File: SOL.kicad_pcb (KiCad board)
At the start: 2 copper layers, 50.8 x 31.8 mm, 4 parts, among them J2 Conn_Coaxial, J3 Conn_Coaxial, J4 Conn_Coaxial

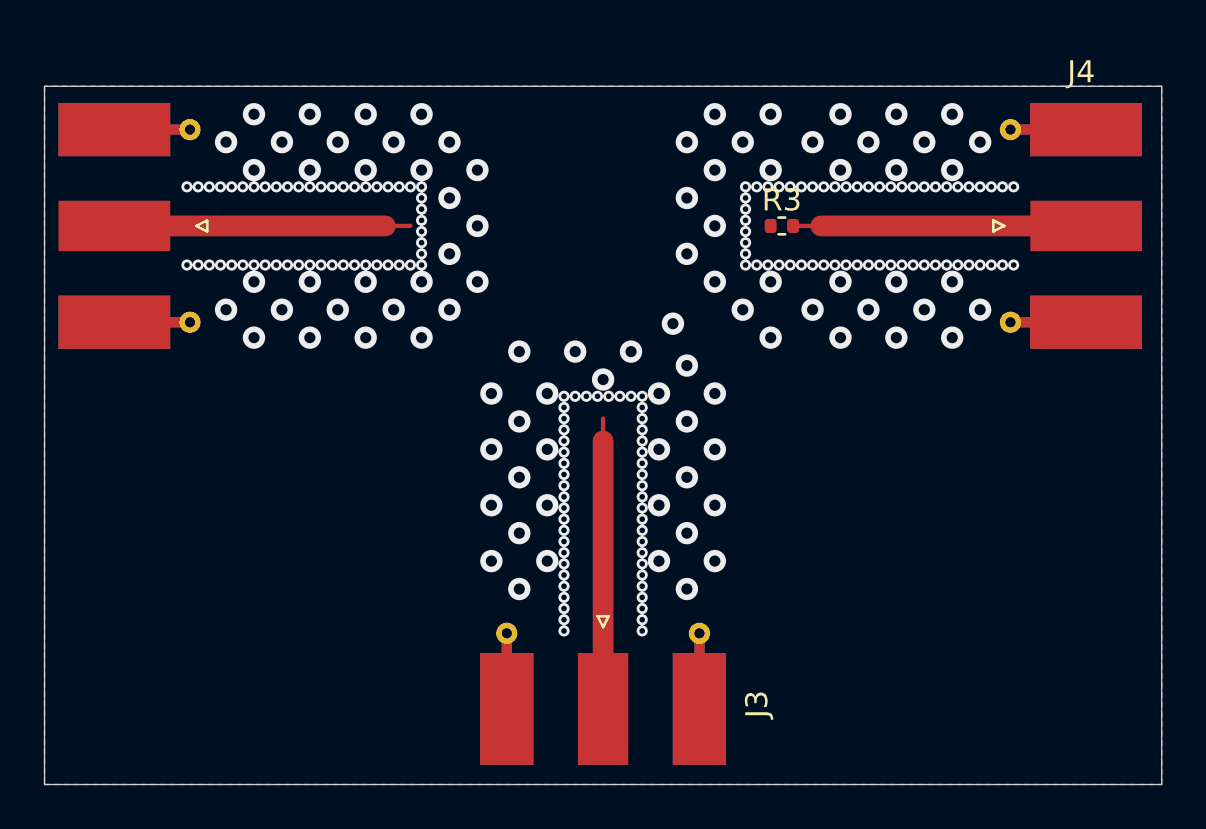
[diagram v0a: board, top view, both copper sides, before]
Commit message: updated SMA launch to SW microwave on all boards
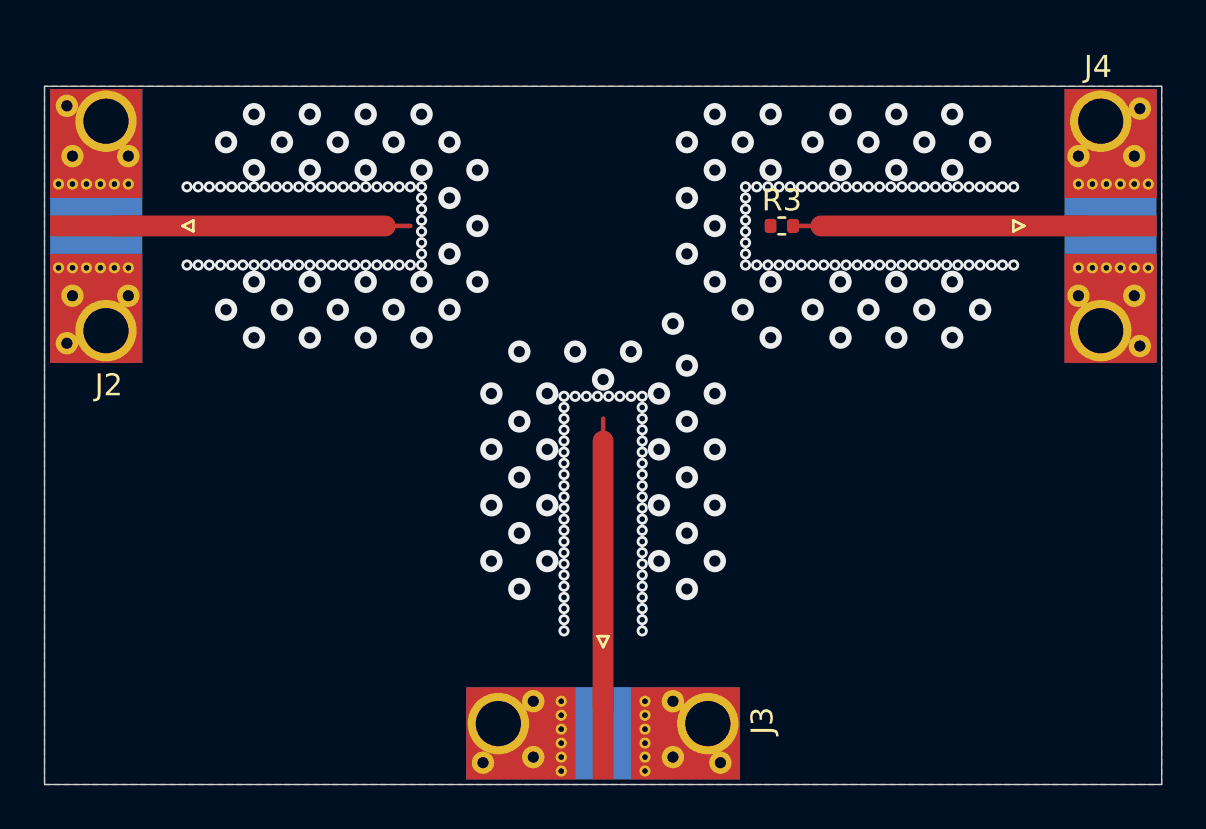
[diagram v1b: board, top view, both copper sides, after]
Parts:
- J2, J3, J4: footprint Connector_Coaxial:SMA_Molex_73251-1153_EdgeMount_Horizontal -> southwest-microwave-connectors:southwest-super-SMA-292-04A-12
- moved J3 5.18 mm to (175.4, 150.8)
- moved J4 5.18 mm to (200.8, 125.4)
- moved J2 4.90 mm to (150.0, 125.4)

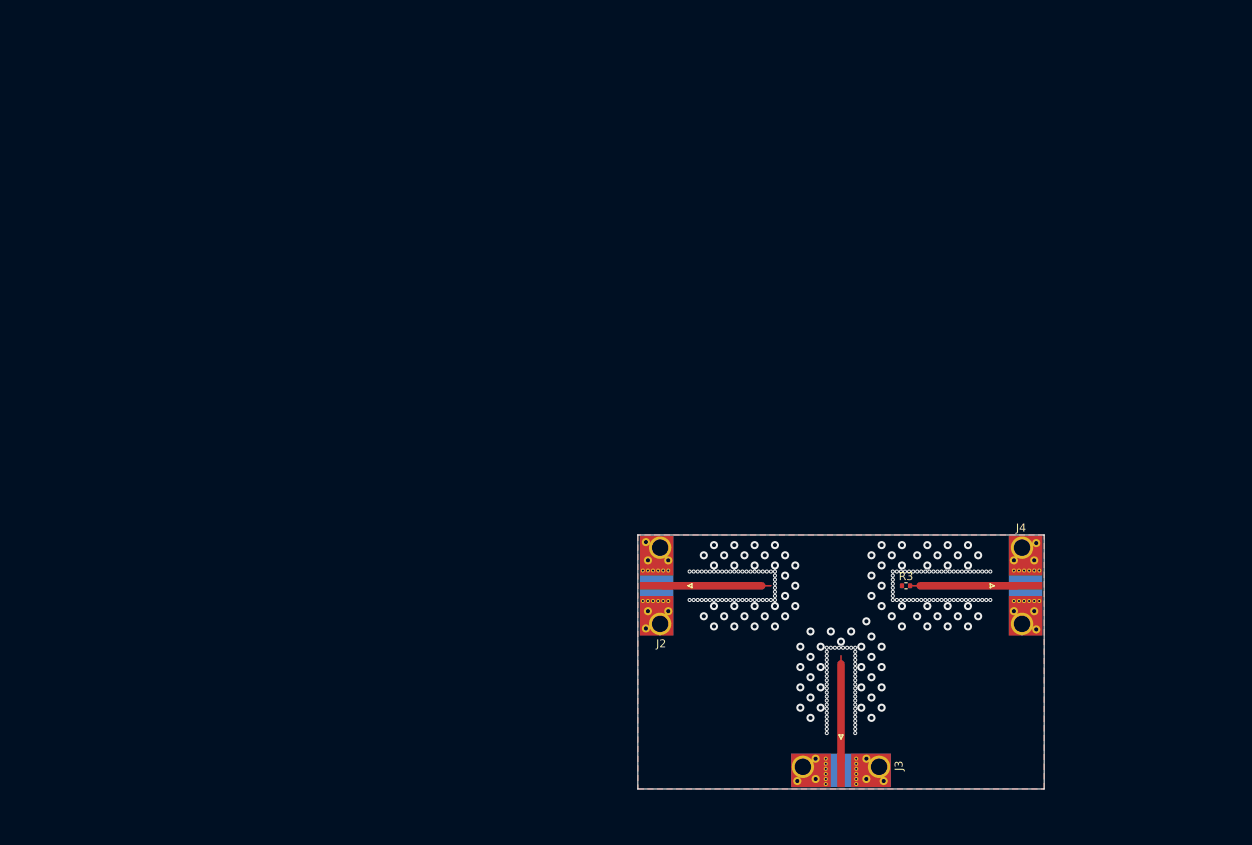
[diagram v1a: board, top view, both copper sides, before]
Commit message: used altium files to build kicad models of mm5800 and started new twpatron
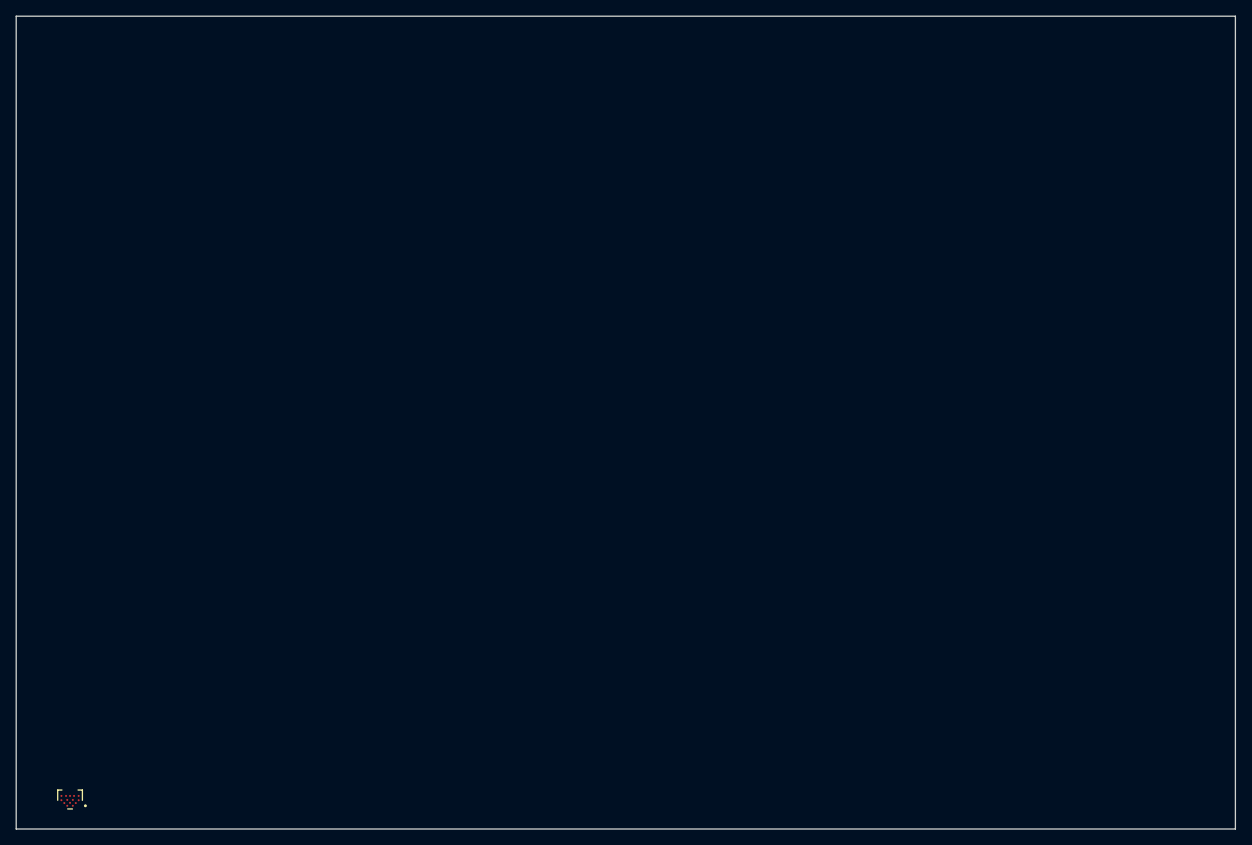
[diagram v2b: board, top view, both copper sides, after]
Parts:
- removed J2, J3, J4: Conn_Coaxial, southwest-microwave-connectors:southwest-super-SMA-292-04A-12
- removed R3: 50, Resistor_SMD:R_0402_1005Metric
- added Designator237: Comment, Menlo_Altium_Library:MM5800, F.Cu at (79.0, 152.1)
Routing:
- net GND: track 13.5 -> 0.00 mm, vias 250 -> 0
- net unconnected-(J3-In-Pad1): track 13.2 -> 0.00 mm
- net Net-(J4-In): track 13.2 -> 0.00 mm
- removed copper zone on B.Cu, net GND
- removed copper zone on F.Cu, net GND
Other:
- board size 50.8 x 31.8 mm -> 152.4 x 101.6 mm
- rule pad_to_mask_clearance: 0 -> 0.1016
